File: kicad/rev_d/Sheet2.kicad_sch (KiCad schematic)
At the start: 159 parts, among them J10 vg_old, J5 external clock, J6 JUMPER, J8 JUMPER, J9 JUMPER, Q2 QUARTZ, Q3 QUARTZ32768, X11 KEYB-MOUSE, X12 IDC20, X13 USB_C, X15 PLB2-2, X19 AVR pgm conn, X4 IDC10M, X5 IDC10M, X6 RS232_9

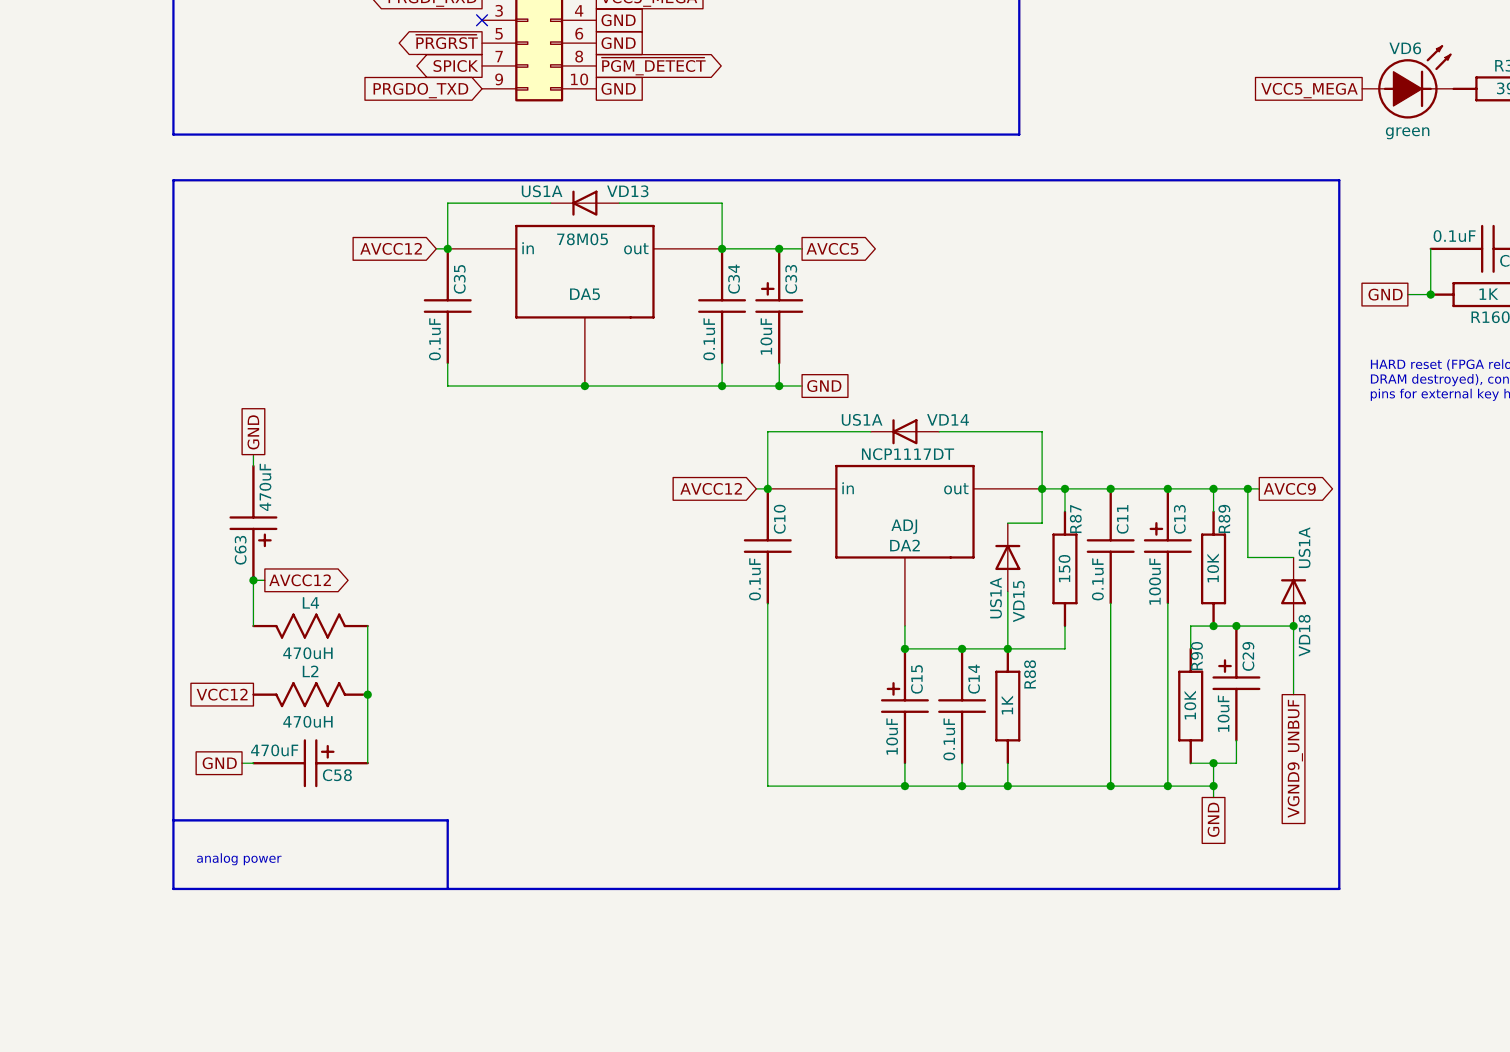
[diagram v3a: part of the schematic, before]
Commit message: pentevo: rev D: start redoing audio part (WIP)
git-svn-id: svn://localhost/local-pentevo@1222 c6c76956-fad2-4150-a3a9-ea0a427205ba
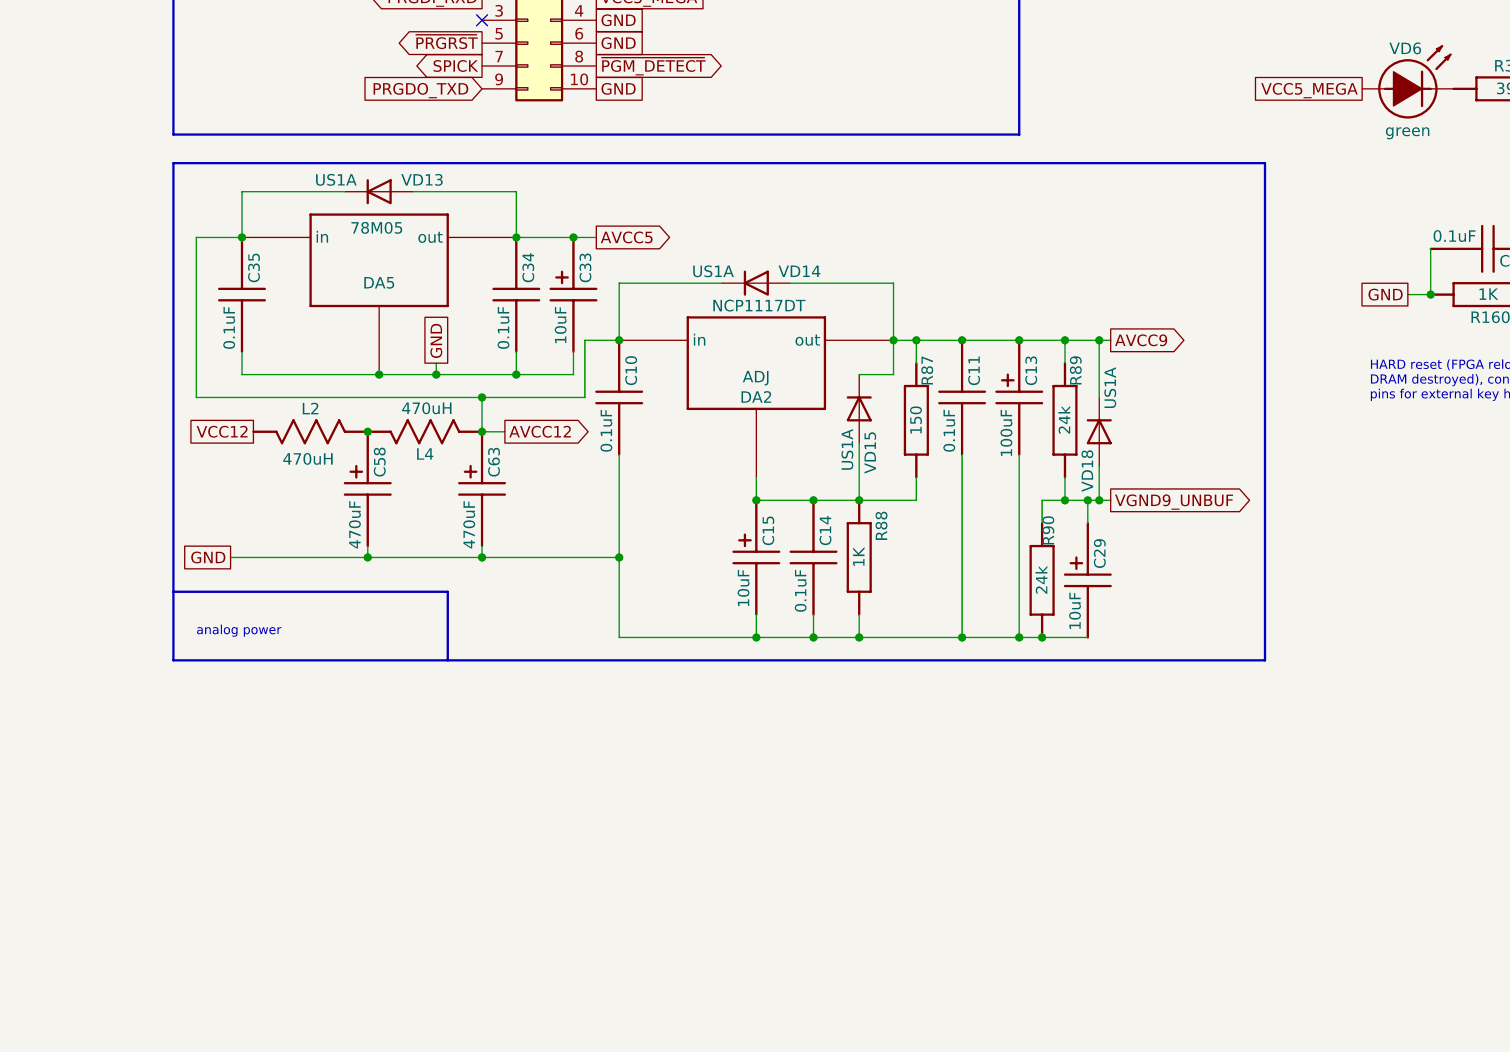
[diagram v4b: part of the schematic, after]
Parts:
- R89, R90: value 10K -> 24k
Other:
- moved on the sheet: C10, C11, C13, C14, C15, C29, C33, C34, C35, C58, C63, DA2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

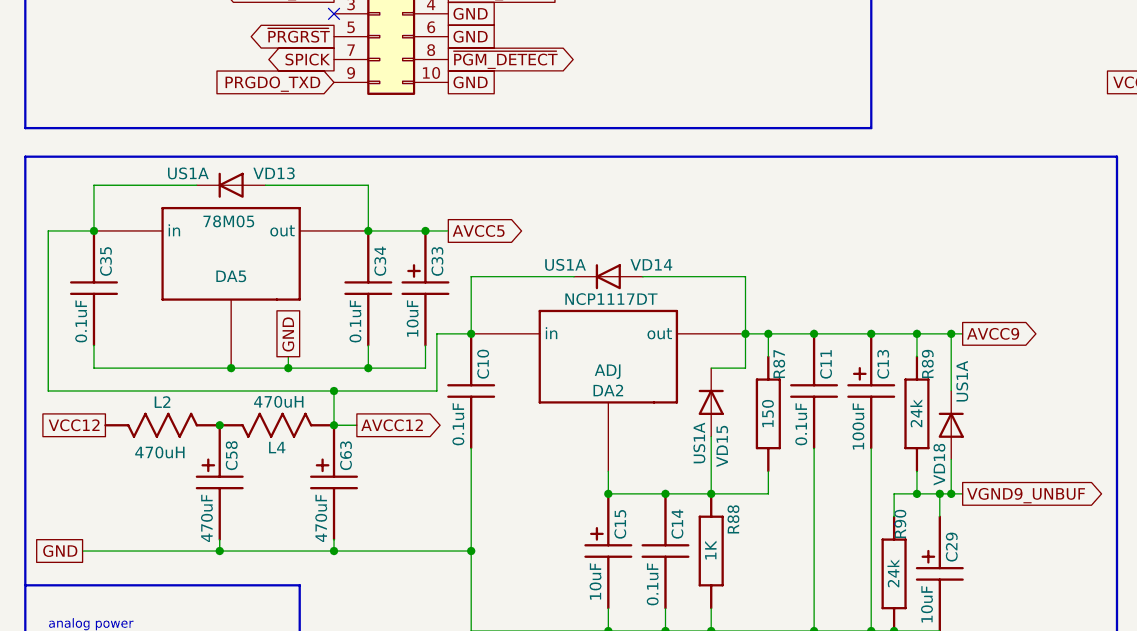
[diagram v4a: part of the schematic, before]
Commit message: pentevo: add datasheets for SS14 and S1A diodes; rev. D: replace linear regulator diodes with S1A
git-svn-id: svn://localhost/local-pentevo@1223 c6c76956-fad2-4150-a3a9-ea0a427205ba
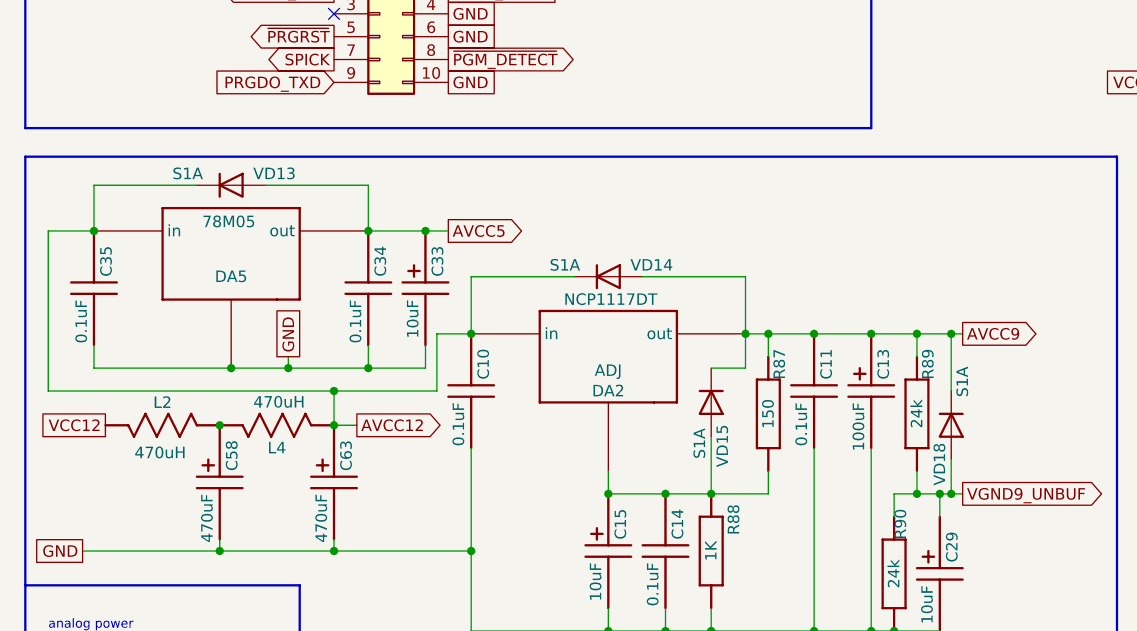
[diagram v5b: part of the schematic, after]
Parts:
- VD13, VD14, VD15, VD18: value US1A -> S1A
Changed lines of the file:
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@@
 			)
 		)
-		(property "Value" "US1A"
+		(property "Value" "S1A"
 			(at 141.224 210.82 0)
 			(effects
@@
 			)
 		)
-		(property "Value" "US1A"
+		(property "Value" "S1A"
 			(at 99.314 200.66 0)
 			(effects
@@
 			)
 		)
-		(property "Value" "US1A"
+		(property "Value" "S1A"
 			(at 185.42 223.774 0)
 			(effects
@@
 			)
 		)
-		(property "Value" "US1A"
+		(property "Value" "S1A"
 			(at 156.21 230.632 0)
 			(effects

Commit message: pentevo: rev D: add pca9555 to control extra address pins of ROM
git-svn-id: svn://localhost/local-pentevo@1228 c6c76956-fad2-4150-a3a9-ea0a427205ba
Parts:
- added C122, C123: 0.1uF, C-CHIP, symbol eva-altium-import:Sheet2_0_CAPCHIP
- added D24: '07, SO14, symbol eva-altium-import:Sheet1_0_07
- added R186, R187, R188, R189: 10K, R-CHIP, symbol eva-altium-import:Sheet2_1_RESCHIP
- added U2: PCA9555DB, Package_SO:SSOP-24_5.3x8.2mm_P0.65mm, symbol Interface_Expansion:PCA9555DB
- added VD20: S1A, Diode_SMD:D_SMA, symbol Diode:US1A
- R22, R23: value 10K -> 4K7
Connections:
- net GND: now also C122.2, C123.2, D24.7 (GND), U2.12 (VSS), U2.2 (A1), U2.21 (A0), U2.3 (A2)
- net SCL: now also U2.22 (SCL)
- net SDA: now also U2.23 (SDA)
- net VCC3V3_uSD: now also VD20.2 (A)
- net VCC5: now also R186.1 (i/o), R187.1 (i/o), R188.1 (i/o)
- net VCC5_MEGA: now also C122.1, C123.1, D24.14 (+5V), R189.2 (i/o1), U2.24 (VDD), VD20.1 (K)
- new net: D24.1 (A0), U2.18 (IO1_5)
- new net: D24.3 (A1), U2.19 (IO1_6)
- new net: D24.5 (A2), U2.20 (IO1_7)
- new net: D24.11 (A4), D24.13 (A5), D24.9 (A3), R189.1 (i/o)
- new net ROM_STATIC_A19: D24.2 (B0), R186.2 (i/o1)
- new net ROM_STATIC_A20: D24.4 (B1), R187.2 (i/o1)
- new net ROM_STATIC_A21: D24.6 (B2), R188.2 (i/o1)
- no-connect marks 22 -> 26
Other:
- moved on the sheet: J6, J8, R144

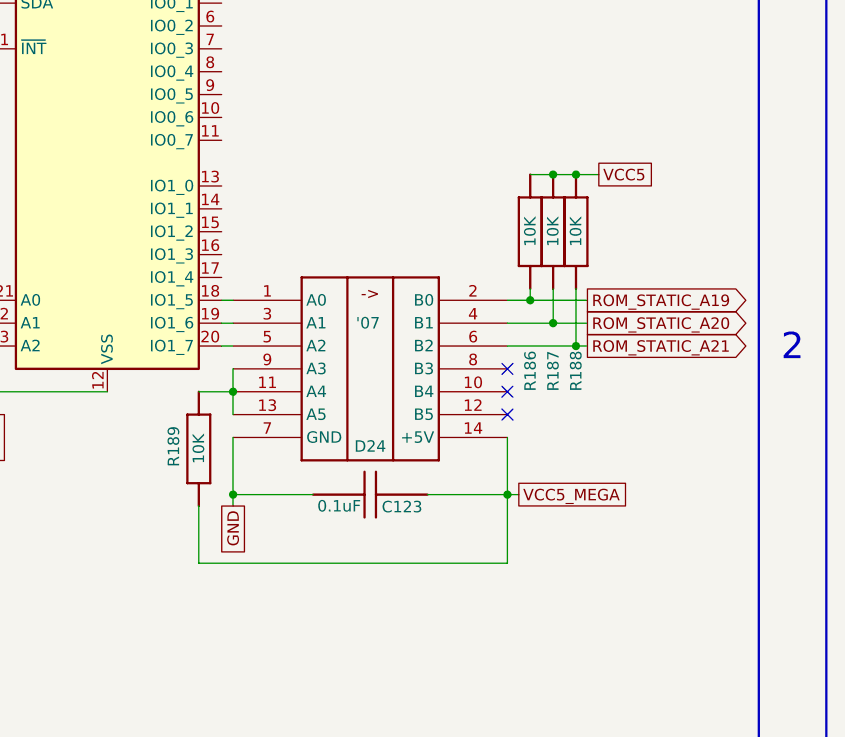
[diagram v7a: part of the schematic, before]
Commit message: pentevo: rev D: beautify audio schematics page, change vcc_mega to vcc5 convertor for high ROM addrs
git-svn-id: svn://localhost/local-pentevo@1258 c6c76956-fad2-4150-a3a9-ea0a427205ba
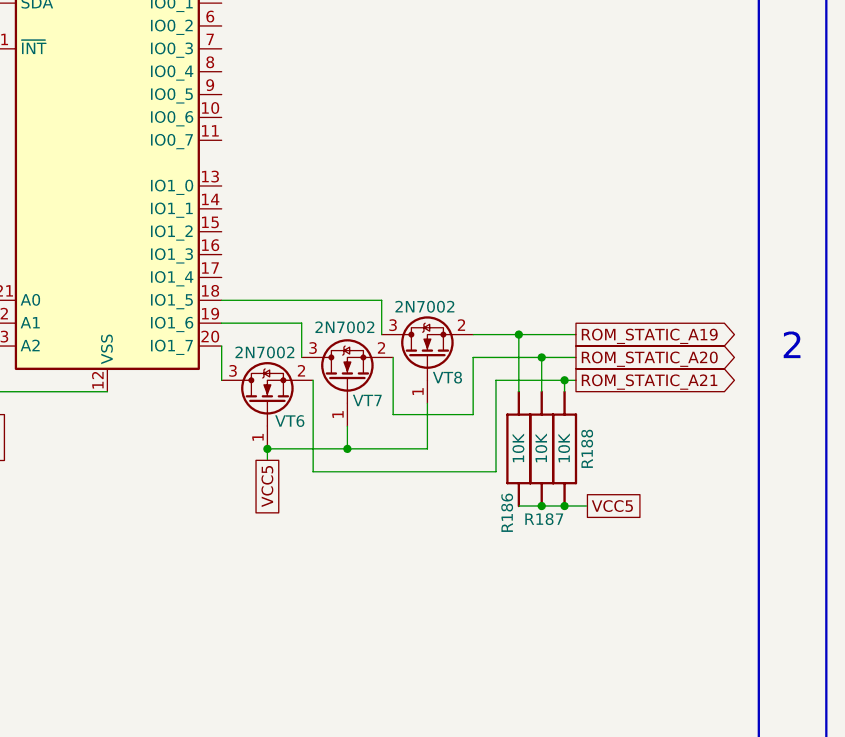
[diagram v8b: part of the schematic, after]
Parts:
- removed C123: 0.1uF, C-CHIP, symbol eva-altium-import:Sheet2_0_CAPCHIP
- removed D24: '07, SO14, symbol eva-altium-import:Sheet1_0_07
- removed R189: 10K, R-CHIP, symbol eva-altium-import:Sheet2_1_RESCHIP
- added VT6, VT7, VT8: 2N7002, Package_TO_SOT_SMD:SOT-23, symbol Transistor_FET:2N7002
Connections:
- net ROM_STATIC_A19: now also VT8.2 (S)
- net ROM_STATIC_A20: now also VT7.2 (S)
- net ROM_STATIC_A21: now also VT6.2 (S)
- net VCC5: now also VT6.1 (G), VT7.1 (G), VT8.1 (G)
- net at U2.18 (IO1_5): now also VT8.3 (D)
- net at U2.19 (IO1_6): now also VT7.3 (D)
- net at U2.20 (IO1_7): now also VT6.3 (D)
- no-connect marks 26 -> 23
